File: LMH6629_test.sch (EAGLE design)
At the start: 6 parts, among them X1 1-227161-0

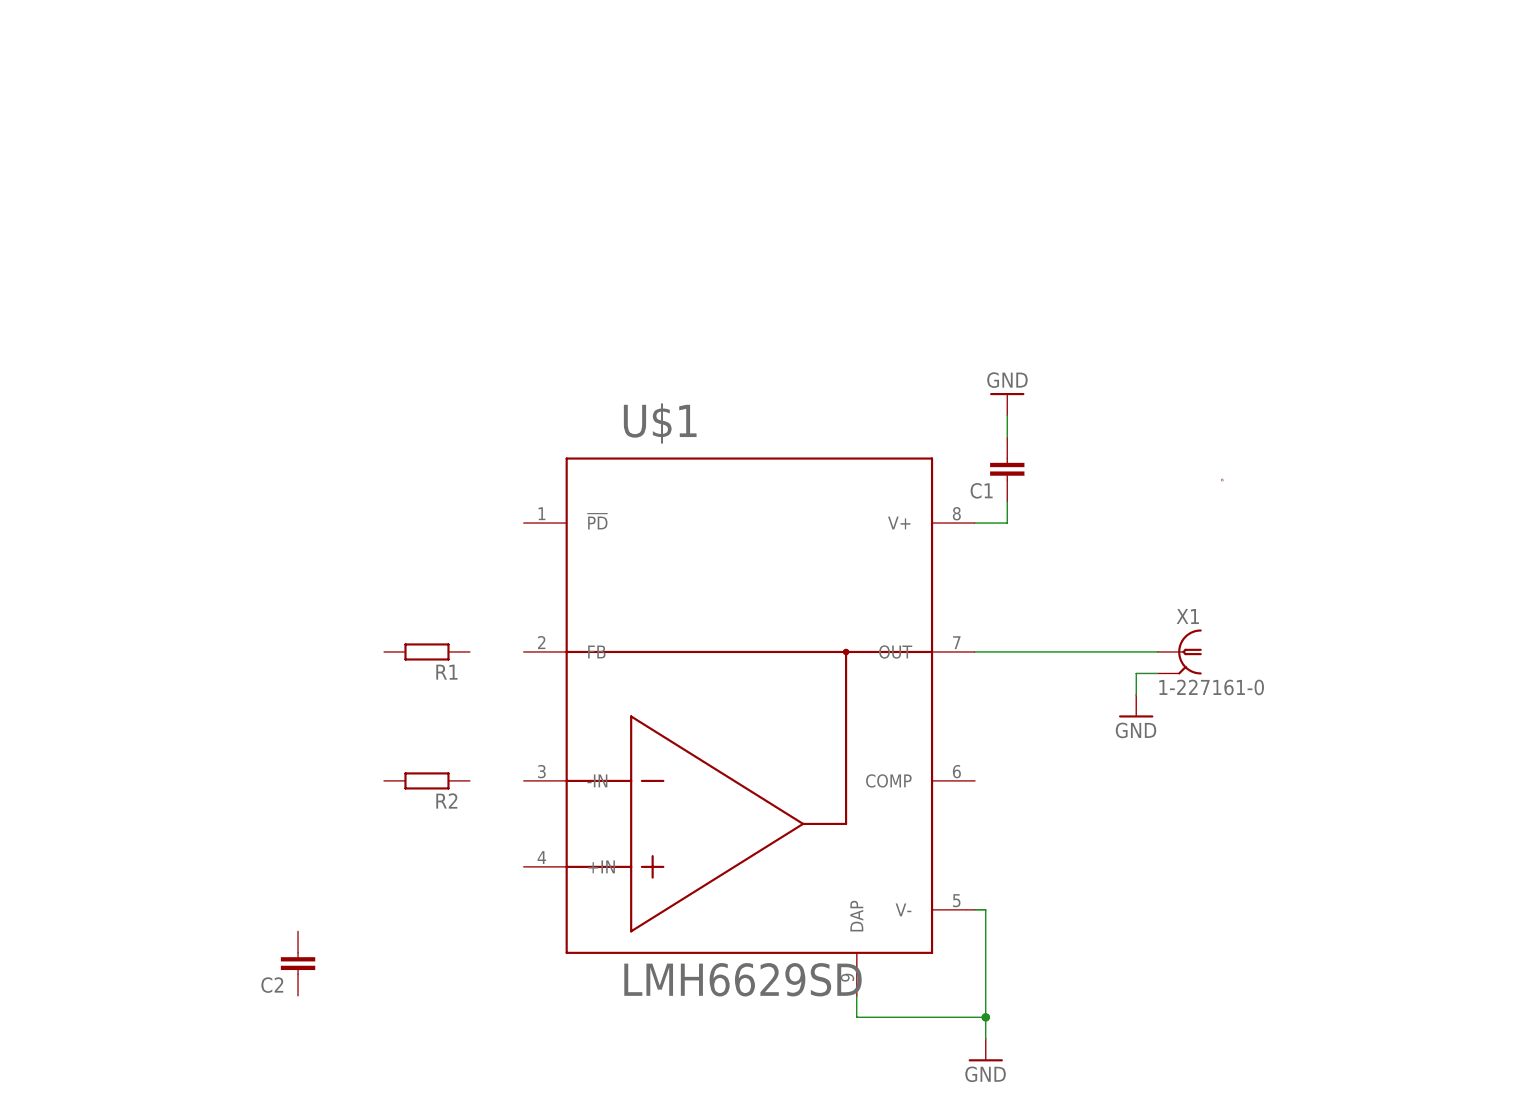
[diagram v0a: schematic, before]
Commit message: add NCP5661
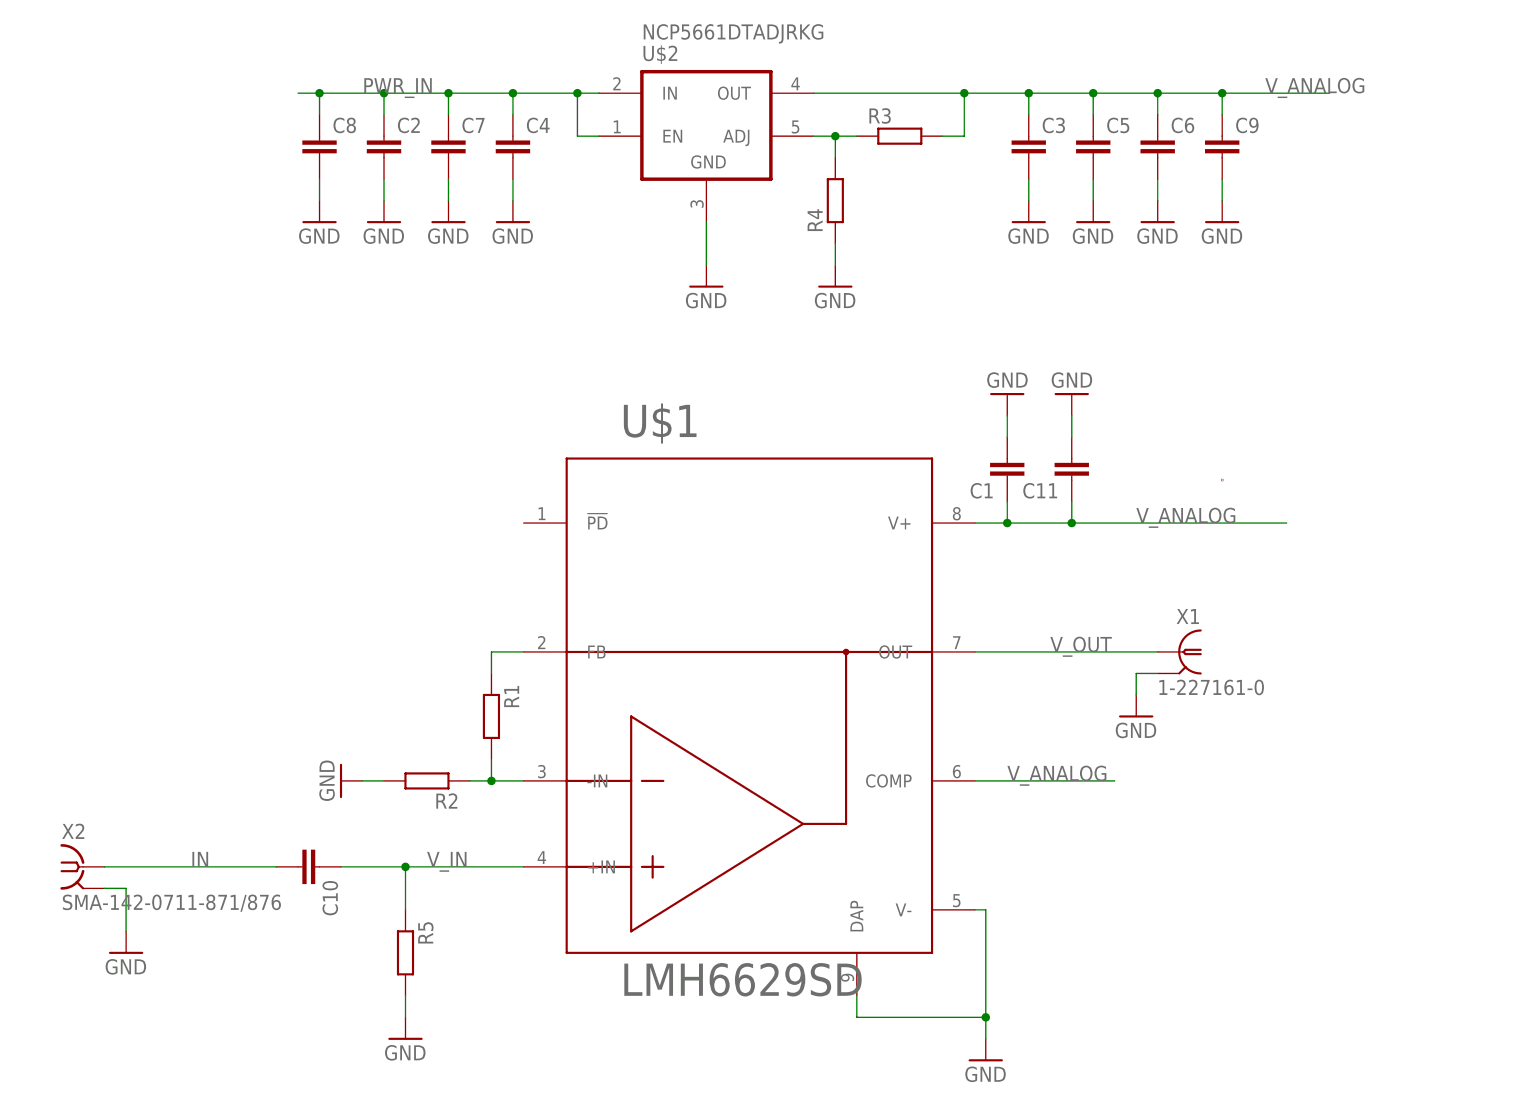
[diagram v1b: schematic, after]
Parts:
- added C10, C11, C3, C4, C5, C7: (no value), rcl:C-EUC0603
- added C6, C8, C9: (no value), rcl:C-EUC0805
- added R3, R4, R5: (no value), resistor:R-EU_R0603
- added U$2: NCP5661DTADJRKG, on-semi:NCP5661DTADJRKG
- added X2: SMA-142-0711-871/876, con-coax:SMA-142-0711-871/876
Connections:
- net N$1 renamed V_OUT
- removed net N$3: C1.1, U$1.V+
- new net IN: C10.2, X2.1
- new net N$4: R3.1, R4.2, U$2.ADJ
- new net N$5: R1.2, R2.1, U$1.-IN
- new net N$6: R1.1, U$1.FB
- new net PWR_IN: C2.1, C4.1, C7.1, C8.1, U$2.EN, U$2.IN
- new net V_ANALOG: C1.1, C11.1, C3.1, C5.1, C6.1, C9.1, R3.2, U$1.COMP, U$1.V+, U$2.OUT
- new net V_IN: C10.1, R5.1, U$1.+IN
- net GND: now also C11.2, C2.2, C3.2, C4.2, C5.2, C6.2, C7.2, C8.2, C9.2, R2.2, R4.1, R5.2, U$2.GND, X2.2
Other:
- moved on the sheet: C2, R1

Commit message: some progress on pcb
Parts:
- removed C5: (no value), rcl:C-EUC0603
- removed C9: (no value), rcl:C-EUC0805
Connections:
- net N$4 renamed ADJ
- net GND: no longer C5.2, C9.2
- net V_ANALOG: no longer C5.1, C9.1
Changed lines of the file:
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@@
 <?xml version="1.0" encoding="utf-8"?>
 <!DOCTYPE eagle SYSTEM "eagle.dtd">
-<eagle version="8.3.2">
+<eagle version="8.4.3">
 <drawing>
 <settings>
@@
 <setting verticaltext="up"/>
 </settings>
-<grid distance="0.1" unitdist="inch" unit="inch" style="dots" multiple="1" display="yes" altdistance="0.01" altunitdist="inch" altunit="inch"/>
+<grid distance="0.1" unitdist="inch" unit="inch" style="lines" multiple="1" display="yes" altdistance="0.01" altunitdist="inch" altunit="inch"/>
 <layers>
 <layer number="1" name="Top" color="4" fill="1" visible="no" active="no"/>
@@
 <part name="GND8" library="supply1" library_urn="urn:adsk.eagle:library:371" deviceset="GND" device=""/>
 <part name="GND9" library="supply1" library_urn="urn:adsk.eagle:library:371" deviceset="GND" device=""/>
-<part name="C5" library="rcl" library_urn="urn:adsk.eagle:library:334" deviceset="C-EU" device="C0603" package3d_urn="urn:adsk.eagle:package:23616/2"/>
 <part name="C6" library="rcl" library_urn="urn:adsk.eagle:library:334" deviceset="C-EU" device="C0805" package3d_urn="urn:adsk.eagle:package:23617/2"/>
 <part name="C7" library="rcl" library_urn="urn:adsk.eagle:library:334" deviceset="C-EU" device="C0603" package3d_urn="urn:adsk.eagle:package:23616/2"/>
 <part name="C8" library="rcl" library_urn="urn:adsk.eagle:library:334" deviceset="C-EU" device="C0805" package3d_urn="urn:adsk.eagle:package:23617/2"/>
-<part name="C9" library="rcl" library_urn="urn:adsk.eagle:library:334" deviceset="C-EU" device="C0805" package3d_urn="urn:adsk.eagle:package:23617/2"/>
-<part name="GND10" library="supply1" library_urn="urn:adsk.eagle:library:371" deviceset="GND" device=""/>
 <part name="GND11" library="supply1" library_urn="urn:adsk.eagle:library:371" deviceset="GND" device=""/>
-<part name="GND12" library="supply1" library_urn="urn:adsk.eagle:library:371" deviceset="GND" device=""/>
 <part name="GND13" library="supply1" library_urn="urn:adsk.eagle:library:371" deviceset="GND" device=""/>
 <part name="GND14" library="supply1" library_urn="urn:adsk.eagle:library:371" deviceset="GND" device=""/>
@@
 <instance part="GND8" gate="1" x="66.04" y="43.18"/>
 <instance part="GND9" gate="1" x="58.42" y="73.66" rot="R270"/>
-<instance part="C5" gate="G$1" x="147.32" y="149.86"/>
 <instance part="C6" gate="G$1" x="154.94" y="149.86"/>
 <instance part="C7" gate="G$1" x="71.12" y="149.86"/>
 <instance part="C8" gate="G$1" x="55.88" y="149.86"/>
-<instance part="C9" gate="G$1" x="162.56" y="149.86"/>
-<instance part="GND10" gate="1" x="147.32" y="139.7"/>
 <instance part="GND11" gate="1" x="154.94" y="139.7"/>
-<instance part="GND12" gate="1" x="162.56" y="139.7"/>
 <instance part="GND13" gate="1" x="71.12" y="139.7"/>
 <instance part="GND14" gate="1" x="63.5" y="139.7"/>
@@
 </segment>
 <segment>
-<pinref part="GND10" gate="1" pin="GND"/>
-<pinref part="C5" gate="G$1" pin="2"/>
-<wire x1="147.32" y1="142.24" x2="147.32" y2="144.78" width="0.1524" layer="91"/>
-</segment>
-<segment>
 <pinref part="GND11" gate="1" pin="GND"/>
 <pinref part="C6" gate="G$1" pin="2"/>
 <wire x1="154.94" y1="142.24" x2="154.94" y2="144.78" width="0.1524" layer="91"/>
-</segment>
-<segment>
-<pinref part="GND12" gate="1" pin="GND"/>
-<pinref part="C9" gate="G$1" pin="2"/>
-<wire x1="162.56" y1="142.24" x2="162.56" y2="144.78" width="0.1524" layer="91"/>
 </segment>
 <segment>
@@
 </segment>
 </net>
-<net name="N$4" class="0">
+<net name="ADJ" class="0">
 <segment>
 <pinref part="U$2" gate="G$1" pin="ADJ"/>
@@
 <wire x1="139.7" y1="154.94" x2="132.08" y2="154.94" width="0.1524" layer="91"/>
 <junction x="132.08" y="154.94"/>
-<wire x1="175.26" y1="154.94" x2="162.56" y2="154.94" width="0.1524" layer="91"/>
+<wire x1="175.26" y1="154.94" x2="154.94" y2="154.94" width="0.1524" layer="91"/>
 <junction x="139.7" y="154.94"/>
 <label x="167.64" y="154.94" size="1.778" layer="95"/>
-<pinref part="C5" gate="G$1" pin="1"/>
-<wire x1="162.56" y1="154.94" x2="154.94" y2="154.94" width="0.1524" layer="91"/>
-<wire x1="154.94" y1="154.94" x2="147.32" y2="154.94" width="0.1524" layer="91"/>
-<wire x1="147.32" y1="154.94" x2="139.7" y2="154.94" width="0.1524" layer="91"/>
-<wire x1="147.32" y1="152.4" x2="147.32" y2="154.94" width="0.1524" layer="91"/>
-<junction x="147.32" y="154.94"/>
+<wire x1="154.94" y1="154.94" x2="139.7" y2="154.94" width="0.1524" layer="91"/>
 <pinref part="C6" gate="G$1" pin="1"/>
 <wire x1="154.94" y1="152.4" x2="154.94" y2="154.94" width="0.1524" layer="91"/>
 <junction x="154.94" y="154.94"/>
-<pinref part="C9" gate="G$1" pin="1"/>
-<wire x1="162.56" y1="152.4" x2="162.56" y2="154.94" width="0.1524" layer="91"/>
-<junction x="162.56" y="154.94"/>
-</segment>
-<segment>
+</segment>
+<segment>
